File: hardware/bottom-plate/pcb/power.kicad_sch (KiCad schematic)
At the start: 7 parts, among them U2 AMS1084CM-5.0, U3 AMS1084CM-3.3

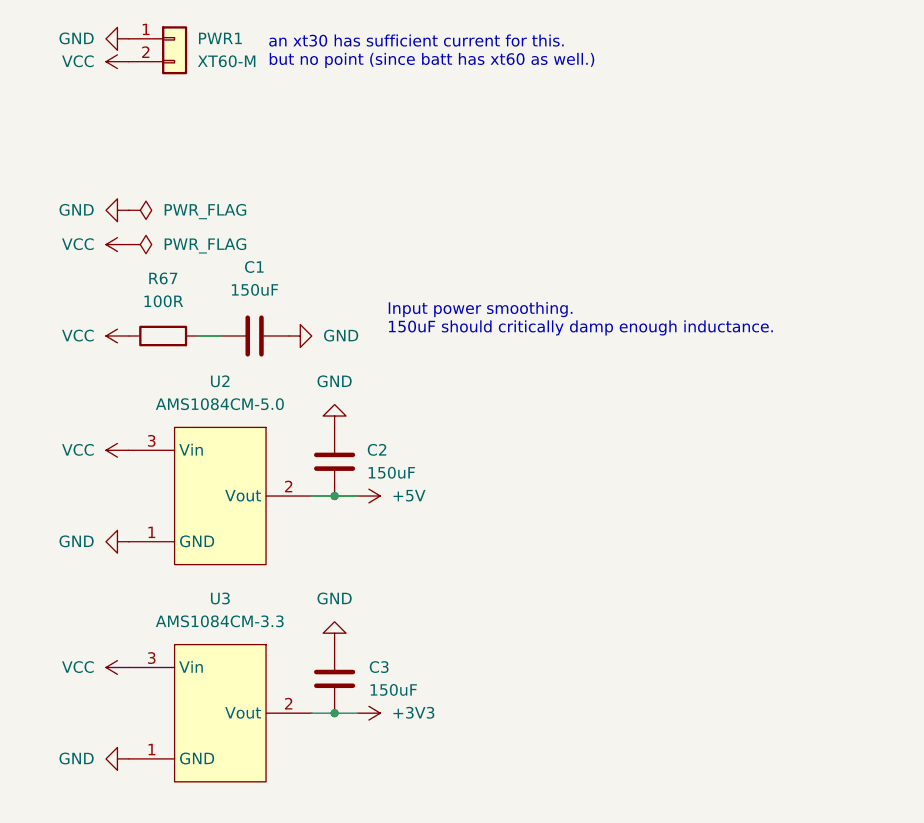
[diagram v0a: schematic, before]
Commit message: kicker pcb done, working on bottom plate
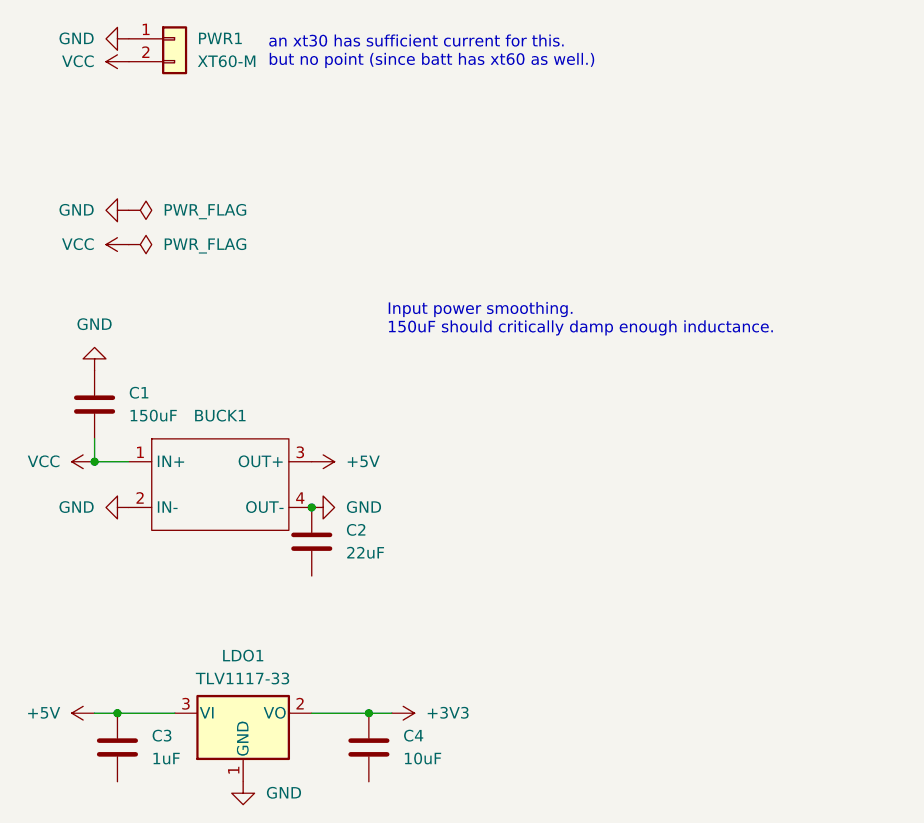
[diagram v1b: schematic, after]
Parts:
- removed R67: 100R, symbol Device:R
- removed U2: AMS1084CM-5.0, Package_TO_SOT_SMD:TO-263-3_TabPin2, symbol EasyEDA:AMS1084CM-5.0
- removed U3: AMS1084CM-3.3, Package_TO_SOT_SMD:TO-263-3_TabPin2, symbol EasyEDA:AMS1084CM-3.3
- added BUCK1: ~, custom:mini560, symbol custom:mini360/560
- added C4: 10uF, PCM_Capacitor_SMD_AKL:C_0805_2012Metric_Pad1.15x1.40mm_HandSolder, symbol Device:C
- added LDO1: TLV1117-33, Package_TO_SOT_SMD:SOT-223-3_TabPin2, symbol Regulator_Linear:TLV1117-33
- C2: value 150uF -> 22uF; footprint Capacitor_SMD:CP_Elec_6.3x7.7 -> PCM_Capacitor_SMD_AKL:C_0805_2012Metric_Pad1.15x1.40mm_HandSolder
- C3: value 150uF -> 1uF; footprint Capacitor_SMD:CP_Elec_6.3x7.7 -> PCM_Capacitor_SMD_AKL:C_0805_2012Metric_Pad1.15x1.40mm_HandSolder
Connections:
- net +3V3: now also C4.2, LDO1.2 (VO); no longer C3.1
- net +5V: now also C3.2, BUCK1.3 (OUT+), LDO1.3 (VI); no longer C2.1
- net GND: now also C1.1, C2.1, BUCK1.2 (IN-), BUCK1.4 (OUT-), LDO1.1 (GND); no longer C1.2, C2.2, C3.2
- net VCC: now also C1.2, BUCK1.1 (IN+)
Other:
- moved on the sheet: C1

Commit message: cleaned up bottom plate schematic and added explanations of design decisions. Please read.
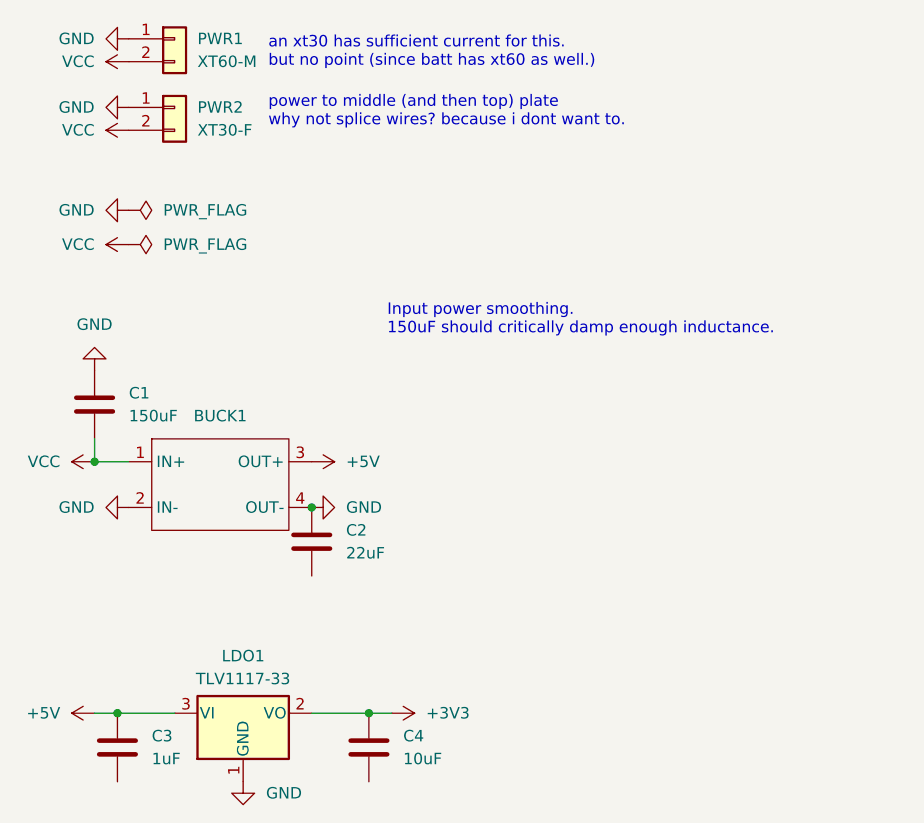
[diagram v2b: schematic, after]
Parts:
- added PWR2: XT30-F, Connector_AMASS:AMASS_XT30U-F_1x02_P5.0mm_Vertical, symbol Connector_Generic:Conn_01x02
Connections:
- net GND: now also PWR2.1 (Pin_1)
- net VCC: now also PWR2.2 (Pin_2)
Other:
- note added: "power to middle (and then top) plate why not splice wires? because i dont want to."
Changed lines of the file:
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@@
+		)
+	)
+	(text "power to middle (and then top) plate\nwhy not splice wires? because i dont want to."
+		(exclude_from_sim no)
+		(at 40.894 27.178 0)
+		(effects
+			(font
+				(size 1.27 1.27)
+			)
+			(justify left)
 		)
 	)
@@
 	)
 	(symbol
+		(lib_id "Connector_Generic:Conn_01x02")
+		(at 30.48 26.67 0)
+		(unit 1)
+		(exclude_from_sim no)
+		(in_bom yes)
+		(on_board yes)
+		(dnp no)
+		(fields_autoplaced yes)
+		(property "Reference" "PWR2"
+			(at 33.02 26.6699 0)
+			(effects
+				(font
+					(size 1.27 1.27)
+				)
+				(justify left)
+			)
+		)
+		(property "Value" "XT30-F"
+			(at 33.02 29.2099 0)
+			(effects
+				(font
+					(size 1.27 1.27)
+				)
+				(justify left)
+			)
+		)
+		(property "Footprint" "Connector_AMASS:AMASS_XT30U-F_1x02_P5.0mm_Vertical"
+			(at 30.48 26.67 0)
+			(effects
+				(font
+					(size 1.27 1.27)
+				)
+				(hide yes)
+			)
+		)
+		(property "Datasheet" "~"
+			(at 30.48 26.67 0)
+			(effects
+				(font
+					(size 1.27 1.27)
+				)
+				(hide yes)
+			)
+		)
+		(property "Description" "Generic connector, single row, 01x02, script generated (kicad-library-utils/schlib/autogen/connector/)"
+			(at 30.48 26.67 0)
+			(effects
+				(font
+					(size 1.27 1.27)
+				)
+				(hide yes)
+			)
+		)
+		(pin "1"
+		)
+		(pin "2"
+		)
+		(instances
+			(project "pcb"
+				(path "/7e6d4b79-c480-4b70-bccc-d28260cddf7c/1bedd62e-fca9-4c03-aeeb-1f89b1b954bd"
+					(reference "PWR2")
+					(unit 1)
+				)
+			)
+		)
+	)
+	(symbol
+		(lib_id "power:+12V")
+		(at 25.4 29.21 90)
+		(unit 1)
+		(exclude_from_sim no)
+		(in_bom yes)
+		(on_board yes)
+		(dnp no)
+		(fields_autoplaced yes)
+		(property "Reference" "#PWR0170"
+			(at 29.21 29.21 0)
+			(effects
+				(font
+					(size 1.27 1.27)
+				)
+				(hide yes)
+			)
+		)
+		(property "Value" "VCC"
+			(at 21.59 29.2099 90)
+			(effects
+				(font
+					(size 1.27 1.27)
+				)
+				(justify left)
+			)
+		)
+		(property "Footprint" ""
+			(at 25.4 29.21 0)
+			(effects
+				(font
+					(size 1.27 1.27)
+				)
+				(hide yes)
+			)
+		)
+		(property "Datasheet" ""
+			(at 25.4 29.21 0)
+			(effects
+				(font
+					(size 1.27 1.27)
+				)
+				(hide yes)
+			)
+		)
+		(property "Description" "Power symbol creates a global label with name \"+12V\""
+			(at 25.4 29.21 0)
+			(effects
+				(font
+					(size 1.27 1.27)
+				)
+				(hide yes)
+			)
+		)
+		(pin "1"
+		)
+		(instances
+			(project "pcb"
+				(path "/7e6d4b79-c480-4b70-bccc-d28260cddf7c/1bedd62e-fca9-4c03-aeeb-1f89b1b954bd"
+					(reference "#PWR0170")
+					(unit 1)
+				)
+			)
+		)
+	)
+	(symbol
 		(lib_id "power:GND")
 		(at 21.59 55.88 180)
@@
 					(unit 1)
 				)
+			)
+		)
+	)
+	(symbol
+		(lib_id "power:GND")
+		(at 25.4 26.67 270)
+		(unit 1)
+		(exclude_from_sim no)
+		(in_bom yes)
+		(on_board yes)
+		(dnp no)
+		(fields_autoplaced yes)
+		(property "Reference" "#PWR0167"
+			(at 19.05 26.67 0)
+			(effects
+				(font
+					(size 1.27 1.27)
+				)
+				(hide yes)
+			)
+		)
+		(property "Value" "GND"
+			(at 21.59 26.6699 90)
+			(effects
+				(font
+					(size 1.27 1.27)
+				)
+				(justify right)
+			)
+		)
+		(property "Footprint" ""
+			(at 25.4 26.67 0)
+			(effects
+				(font
+					(size 1.27 1.27)
+				)
+				(hide yes)
+			)
+		)
+		(property "Datasheet" ""
+			(at 25.4 26.67 0)
+			(effects
+				(font
+					(size 1.27 1.27)
+				)
+				(hide yes)
+			)
+		)
+		(property "Description" "Power symbol creates a global label with name \"GND\" , ground"
+			(at 25.4 26.67 0)
+			(effects
+				(font
+					(size 1.27 1.27)
+				)
+				(hide yes)
+			)
+		)
+		(pin "1"
+		)
+		(instances
+			(project "pcb"
+				(path "/7e6d4b79-c480-4b70-bccc-d28260cddf7c/1bedd62e-fca9-4c03-aeeb-1f89b1b954bd"
+					(reference "#PWR0167")
+					(unit 1)
+				)
